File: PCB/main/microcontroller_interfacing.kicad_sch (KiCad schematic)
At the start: 19 parts, among them U3 CH340G, U4 USB_Micro_B, U5 AT24C256C-SSHL-T, X1 12MHz Crystal

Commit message: Updated BOM
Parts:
- C4, C6: footprint Footprint_EEE3088F:C0402 -> Capacitor_SMD:C_0402_1005Metric; Price $0.0012 -> 0.0012
- C5: JLC Part # C1525 -> C15195; Price $0.0011 -> 0.0011
- C7: Price $0.0011 -> 0.0011
- D8: Price $0.0032 -> 0.0032
- R10: footprint Footprint_EEE3088F:R0603 -> Resistor_SMD:R_0603_1608Metric; Price $0.0014 -> 0.0015
- R11, R12: footprint Footprint_EEE3088F:R0402 -> Resistor_SMD:R_0402_1005Metric; Price $0.0007 -> 0.0007
- R8: footprint Footprint_EEE3088F:R0603 -> Resistor_SMD:R_0402_1005Metric; JLC Part # C23255 -> C25885; Price $0.0014 -> 0.0007
- R9: footprint Footprint_EEE3088F:R0603 -> Resistor_SMD:R_0402_1005Metric; JLC Part # C23255 -> C25900; Price $0.0014 -> 0.0007
- U3: Price $0.5856 -> $0.5838
- U4: JLC Part # C319160 -> C404969; Price $0.0673 -> 0.0491
- U5: Price $1.5556 -> 1.5556
- X1: Price $0.1054 -> 0.1054
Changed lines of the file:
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@@
       (effects (font (size 1.27 1.27)) (justify left))
     )
-    (property "Footprint" "Footprint_EEE3088F:C0402" (id 2) (at 52.4002 113.665 0)
+    (property "Footprint" "Capacitor_SMD:C_0402_1005Metric" (id 2) (at 52.4002 113.665 0)
       (effects (font (size 1.27 1.27)) hide)
     )
@@
       (effects (font (size 1.27 1.27)) hide)
     )
-    (property "Price" "$0.0012" (id 5) (at 51.435 109.855 0)
+    (property "Price" "0.0012" (id 5) (at 51.435 109.855 0)
       (effects (font (size 1.27 1.27)) hide)
     )
@@
       (effects (font (size 1.27 1.27)) hide)
     )
-    (property "JLC Part #" "C319160" (id 5) (at 139.7 43.18 0)
-      (effects (font (size 1.27 1.27)) hide)
-    )
-    (property "Price" "$0.0673" (id 6) (at 139.7 43.18 0)
+    (property "JLC Part #" "C404969" (id 5) (at 139.7 43.18 0)
+      (effects (font (size 1.27 1.27)) hide)
+    )
+    (property "Price" "0.0491" (id 6) (at 139.7 43.18 0)
       (effects (font (size 1.27 1.27)) hide)
     )
@@
       (effects (font (size 1.27 1.27)) hide)
     )
-    (property "Datasheet" "~" (id 3) (at 226.06 29.21 0)
+    (property "Datasheet" "" (id 3) (at 226.06 29.21 0)
       (effects (font (size 1.27 1.27)) hide)
     )
@@
       (effects (font (size 1.27 1.27)) hide)
     )
-    (property "Price" "$0.0011" (id 5) (at 226.06 29.21 0)
+    (property "Price" "0.0011" (id 5) (at 226.06 29.21 0)
       (effects (font (size 1.27 1.27)) hide)
     )
@@
       (effects (font (size 1.27 1.27)) hide)
     )
-    (property "Price" "$1.5556" (id 6) (at 215.9 47.625 0)
+    (property "Price" "1.5556" (id 6) (at 215.9 47.625 0)
       (effects (font (size 1.27 1.27)) hide)
     )
@@
       (effects (font (size 1.27 1.27)) (justify left))
     )
-    (property "Footprint" "Footprint_EEE3088F:R0603" (id 2) (at 147.447 113.03 90)
+    (property "Footprint" "Resistor_SMD:R_0402_1005Metric" (id 2) (at 147.447 113.03 90)
       (effects (font (size 1.27 1.27)) hide)
     )
@@
       (effects (font (size 1.27 1.27)) hide)
     )
-    (property "JLC Part #" "C23255" (id 4) (at 149.225 113.03 0)
-      (effects (font (size 1.27 1.27)) hide)
-    )
-    (property "Price" "$0.0014" (id 5) (at 149.225 113.03 0)
+    (property "JLC Part #" "C25900" (id 4) (at 149.225 113.03 0)
+      (effects (font (size 1.27 1.27)) hide)
+    )
+    (property "Price" "0.0007" (id 5) (at 149.225 113.03 0)
       (effects (font (size 1.27 1.27)) hide)
     )
@@
       (effects (font (size 1.27 1.27)) hide)
     )
-    (property "Price" "$0.1054" (id 6) (at 65.405 107.315 0)
+    (property "Price" "0.1054" (id 6) (at 65.405 107.315 0)
       (effects (font (size 1.27 1.27)) hide)
     )
@@
       (effects (font (size 1.27 1.27)) (justify left))
     )
-    (property "Footprint" "Footprint_EEE3088F:R0402" (id 2) (at 261.112 31.75 90)
+    (property "Footprint" "Resistor_SMD:R_0402_1005Metric" (id 2) (at 261.112 31.75 90)
       (effects (font (size 1.27 1.27)) hide)
     )
@@
       (effects (font (size 1.27 1.27)) hide)
     )
-    (property "Price" "$0.0007" (id 5) (at 262.89 31.75 0)
+    (property "Price" "0.0007" (id 5) (at 262.89 31.75 0)
       (effects (font (size 1.27 1.27)) hide)
     )
@@
       (effects (font (size 1.27 1.27)) (justify left))
     )
-    (property "Footprint" "Footprint_EEE3088F:R0402" (id 2) (at 248.412 31.75 90)
+    (property "Footprint" "Resistor_SMD:R_0402_1005Metric" (id 2) (at 248.412 31.75 90)
       (effects (font (size 1.27 1.27)) hide)
     )
@@
       (effects (font (size 1.27 1.27)) hide)
     )
-    (property "Price" "$0.0007" (id 5) (at 250.19 31.75 0)
+    (property "Price" "0.0007" (id 5) (at 250.19 31.75 0)
       (effects (font (size 1.27 1.27)) hide)
     )
@@
       (effects (font (size 1.27 1.27)) hide)
     )
-    (property "JLC Part #" "C1525" (id 4) (at 53.975 40.005 0)
-      (effects (font (size 1.27 1.27)) hide)
-    )
-    (property "Price" "$0.0011" (id 5) (at 53.975 40.005 0)
+    (property "JLC Part #" "C15195" (id 4) (at 53.975 40.005 0)
+      (effects (font (size 1.27 1.27)) hide)
+    )
+    (property "Price" "0.0011" (id 5) (at 53.975 40.005 0)
       (effects (font (size 1.27 1.27)) hide)
     )
@@
       (effects (font (size 1.27 1.27)) (justify left))
     )
-    (property "Footprint" "Footprint_EEE3088F:R0603" (id 2) (at 158.242 61.595 90)
+    (property "Footprint" "Resistor_SMD:R_0603_1608Metric" (id 2) (at 158.242 61.595 90)
       (effects (font (size 1.27 1.27)) hide)
     )
@@
       (effects (font (size 1.27 1.27)) hide)
     )
-    (property "Price" "$0.0014" (id 5) (at 160.02 61.595 0)
+    (property "Price" "0.0015" (id 5) (at 160.02 61.595 0)
       (effects (font (size 1.27 1.27)) hide)
     )
@@
       (effects (font (size 1.27 1.27)) (justify left))
     )
-    (property "Footprint" "Footprint_EEE3088F:R0603" (id 2) (at 147.447 97.155 90)
+    (property "Footprint" "Resistor_SMD:R_0402_1005Metric" (id 2) (at 147.447 97.155 90)
       (effects (font (size 1.27 1.27)) hide)
     )
@@
       (effects (font (size 1.27 1.27)) hide)
     )
-    (property "JLC Part #" "C23255" (id 4) (at 149.225 97.155 0)
-      (effects (font (size 1.27 1.27)) hide)
-    )
-    (property "Price" "$0.0014" (id 5) (at 149.225 97.155 0)
+    (property "JLC Part #" "C25885" (id 4) (at 149.225 97.155 0)
+      (effects (font (size 1.27 1.27)) hide)
+    )
+    (property "Price" "0.0007" (id 5) (at 149.225 97.155 0)
       (effects (font (size 1.27 1.27)) hide)
     )
@@
       (effects (font (size 1.27 1.27)) (justify left))
     )
-    (property "Footprint" "Footprint_EEE3088F:C0402" (id 2) (at 57.4802 129.54 0)
+    (property "Footprint" "Capacitor_SMD:C_0402_1005Metric" (id 2) (at 57.4802 129.54 0)
       (effects (font (size 1.27 1.27)) hide)
     )
@@
       (effects (font (size 1.27 1.27)) hide)
     )
-    (property "Price" "$0.0012" (id 5) (at 56.515 125.73 0)
+    (property "Price" "0.0012" (id 5) (at 56.515 125.73 0)
       (effects (font (size 1.27 1.27)) hide)
     )
@@
       (effects (font (size 1.27 1.27)) hide)
     )
-    (property "Price" "$0.5856" (id 6) (at 66.675 60.325 0)
+    (property "Price" "$0.5838" (id 6) (at 66.675 60.325 0)
       (effects (font (size 1.27 1.27)) hide)
     )
@@
       (effects (font (size 1.27 1.27)) hide)
     )
-    (property "Price" "$0.0032" (id 5) (at 160.02 51.435 0)
-      (effects (font (size 1.27 1.27)) hide)
-    )
+    (property "Price" "0.0032" (id 5) (at 160.02 51.435 0)
+      (effects (font (size 1.27 1.27)) hide)
+    )

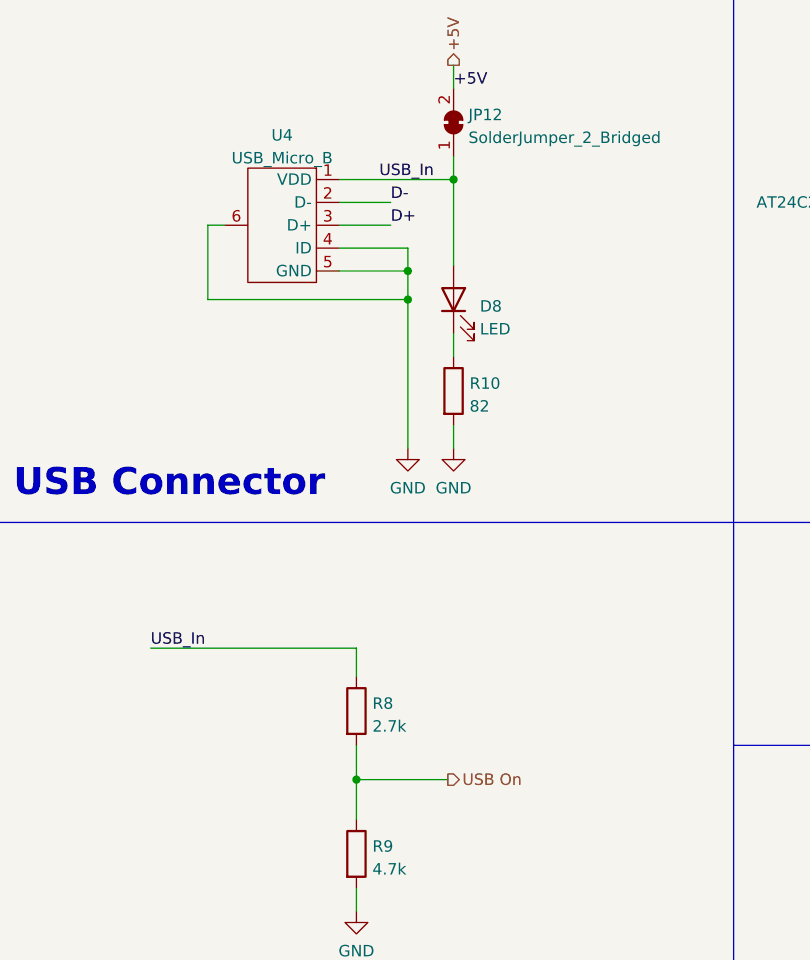
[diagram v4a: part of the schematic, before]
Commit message: Add footprints and test points
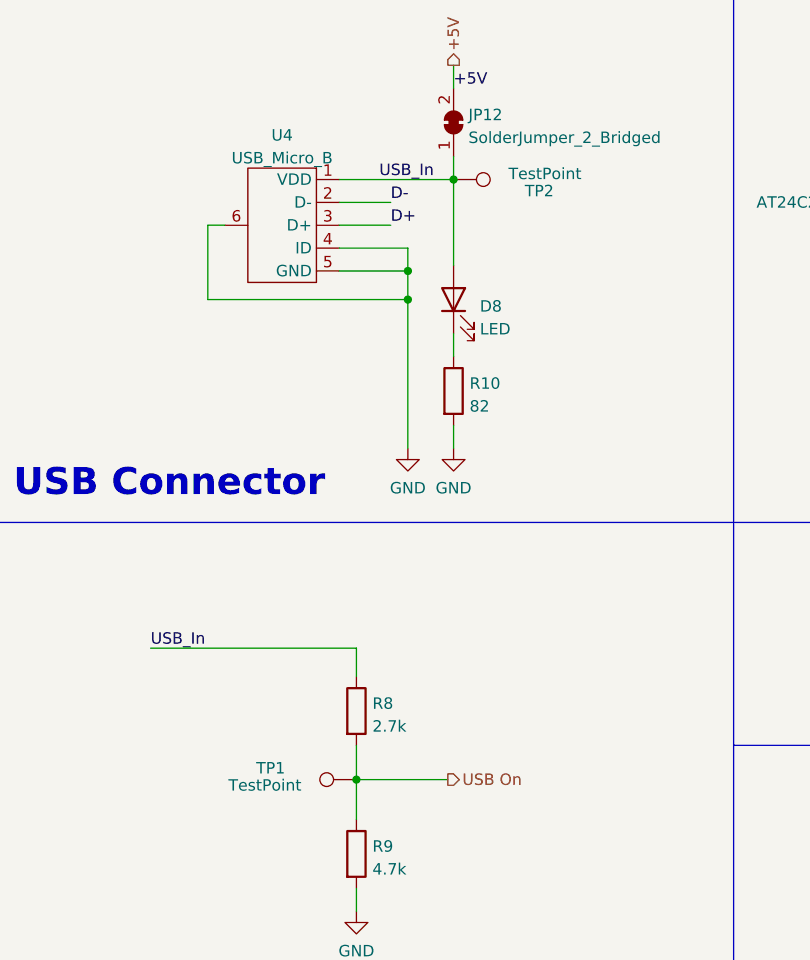
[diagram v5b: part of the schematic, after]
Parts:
- added TP1, TP2: TestPoint, TestPoint:TestPoint_Pad_D1.0mm, symbol Connector:TestPoint
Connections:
- net USB On: now also TP1.1
- net USB_In: now also TP2.1
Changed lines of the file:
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@@
     (pin "2")
+  )
+  (symbol (lib_id "Connector:TestPoint") (at 160.02 38.1 270) (unit 1)
+    (in_bom yes) (on_board yes)
+    (property "Reference" "TP2" (id 0) (at 169.545 39.37 90))
+    (property "Value" "TestPoint" (id 1) (at 170.18 37.465 90))
+    (property "Footprint" "TestPoint:TestPoint_Pad_D1.0mm" (id 2) (at 160.02 43.18 0)
+      (effects (font (size 1.27 1.27)) hide)
+    )
+    (property "Datasheet" "~" (id 3) (at 160.02 43.18 0)
+      (effects (font (size 1.27 1.27)) hide)
+    )
+    (pin "1")
   )
   (symbol (lib_id "Jumper:SolderJumper_2_Bridged") (at 44.45 60.325 0) (unit 1)
@@
     (pin "6")
   )
+  (symbol (lib_id "Connector:TestPoint") (at 149.225 104.775 90) (unit 1)
+    (in_bom yes) (on_board yes)
+    (property "Reference" "TP1" (id 0) (at 139.7 103.505 90))
+    (property "Value" "TestPoint" (id 1) (at 139.065 105.41 90))
+    (property "Footprint" "TestPoint:TestPoint_Pad_D1.0mm" (id 2) (at 149.225 99.695 0)
+      (effects (font (size 1.27 1.27)) hide)
+    )
+    (property "Datasheet" "~" (id 3) (at 149.225 99.695 0)
+      (effects (font (size 1.27 1.27)) hide)
+    )
+    (pin "1")
+  )
   (symbol (lib_id "power:PWR_FLAG") (at 213.995 87.63 0) (unit 1)

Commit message: Design PCB
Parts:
- removed JP12: SolderJumper_2_Bridged, Jumper:SolderJumper-2_P1.3mm_Bridged2Bar_Pad1.0x1.5mm, symbol Jumper:SolderJumper_2_Bridged
- removed TP2: TestPoint, TestPoint:TestPoint_Pad_D1.0mm, symbol Connector:TestPoint
- renumbered C4 to C6, C5 to C7, C6 to C8, C7 to C9, D8 to D4, JP14 to JP10, JP10 to JP7, JP11 to JP8, JP13 to JP9, R8 to R4, R9 to R5, R10 to R6, R11 to R7, R12 to R8, TP1 to TP3
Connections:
- net USB_In is gone; now on net +5V: D4.2 (A), R4.1, U4.1 (VDD)

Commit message: Change names
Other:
- note added: "USB Detector"
- note removed: "USB Dectector"
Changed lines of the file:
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@@
-    (stroke (width 0) (type default) (color 0 0 0 0))
-  )
-  (wire (pts (xy 213.995 87.63) (xy 213.995 90.805))
     (stroke (width 0) (type default) (color 0 0 0 0))
   )
@@
     (stroke (width 0) (type default) (color 0 0 0 0))
   )
-  (text "USB Dectector\n" (at 110.49 140.335 0)
+  (text "USB Detector\n" (at 110.49 140.335 0)
     (effects (font (size 3 3) (thickness 0.8) bold) (justify left bottom))
   )
@@
     (effects (font (size 1.27 1.27)) (justify left bottom))
   )
+  (label "+5V" (at 126.365 90.17 0)
+    (effects (font (size 1.27 1.27)) (justify left bottom))
+  )
   (label "D-" (at 153.035 40.64 0)
     (effects (font (size 1.27 1.27)) (justify left bottom))
@@
     (effects (font (size 1.27 1.27)) (justify left bottom))
   )
-  (label "USB_In" (at 126.365 90.17 0)
-    (effects (font (size 1.27 1.27)) (justify left bottom))
-  )
   (label "D+" (at 153.035 43.18 0)
     (effects (font (size 1.27 1.27)) (justify left bottom))
@@
   )
   (label "D+" (at 38.1 57.785 0)
-    (effects (font (size 1.27 1.27)) (justify left bottom))
-  )
-  (label "+5V" (at 213.995 90.805 270)
-    (effects (font (size 1.27 1.27)) (justify right bottom))
-  )
-  (label "USB_In" (at 151.765 38.1 0)
     (effects (font (size 1.27 1.27)) (justify left bottom))
   )
@@
       (effects (font (size 1.27 1.27)) hide)
     )
-    (pin "1")
-  )
-  (symbol (lib_id "power:PWR_FLAG") (at 213.995 87.63 0) (unit 1)
-    (in_bom yes) (on_board yes) (fields_autoplaced)
-    (property "Reference" "#FLG03" (id 0) (at 213.995 85.725 0)
-      (effects (font (size 1.27 1.27)) hide)
-    )
-    (property "Value" "PWR_FLAG" (id 1) (at 213.995 84.0542 0))
-    (property "Footprint" "" (id 2) (at 213.995 87.63 0)
-      (effects (font (size 1.27 1.27)) hide)
-    )
-    (property "Datasheet" "~" (id 3) (at 213.995 87.63 0)
-      (effects (font (size 1.27 1.27)) hide)
-    )
